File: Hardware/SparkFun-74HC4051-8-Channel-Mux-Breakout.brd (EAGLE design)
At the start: 12.7 x 27.9 mm, 12 parts, among them U1 74HC4051BQ

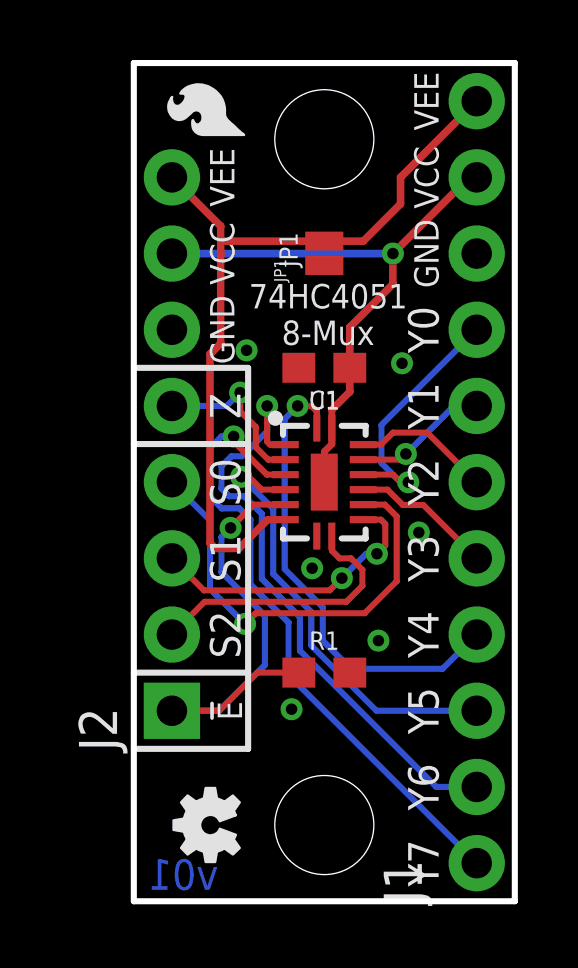
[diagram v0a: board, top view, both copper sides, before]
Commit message: Resolving issues flagged on issue 1.
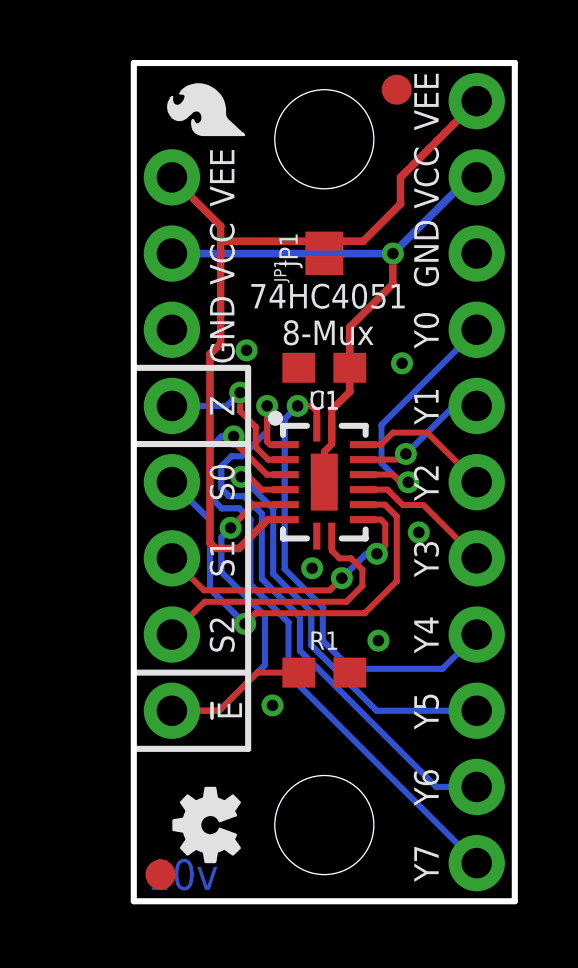
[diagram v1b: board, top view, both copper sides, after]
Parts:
- added FD1, FD2: FIDUCIAL1X2, SparkFun-Aesthetics:FIDUCIAL-1X2
- J1: device SparkFun-Connectors:1X11_NO_SILK -> SparkFun-Connectors:1X11
- J2: device SparkFun-Connectors:1X08_PIN1_NO_SILK -> SparkFun-Connectors:1X08_ROUND
- moved FRAME1 33.6 mm to (-20.3, -12.7)
- flipped J1 to the bottom
- flipped J2 to the bottom
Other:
- board text added: "Jim Lindblom"

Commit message: Few changes after running the checklist.
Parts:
- moved FRAME1 10.9 mm to (-16.5, -22.9)
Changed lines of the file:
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@@
 <wire x1="0" y1="5.08" x2="3.81" y2="5.08" width="0.2032" layer="21"/>
 <wire x1="3.81" y1="5.08" x2="3.81" y2="7.62" width="0.2032" layer="21"/>
-<text x="1.651" y="0.381" size="1.016" layer="16" font="vector" ratio="15" rot="MR0" align="bottom-center">v01</text>
+<text x="1.651" y="0.381" size="1.016" layer="16" font="vector" ratio="20" rot="MR0" align="bottom-center">v01</text>
 <wire x1="0" y1="17.78" x2="3.937" y2="17.78" width="0.2032" layer="22"/>
 <wire x1="3.937" y1="17.78" x2="3.937" y2="15.24" width="0.2032" layer="22"/>
@@
 <wire x1="3.937" y1="5.08" x2="0" y2="5.08" width="0.2032" layer="22"/>
 <wire x1="3.937" y1="5.08" x2="3.937" y2="7.62" width="0.2032" layer="22"/>
-<text x="10.16" y="-12.7" size="1.778" layer="51" font="vector" ratio="15">Jim Lindblom</text>
+<text x="13.97" y="-22.86" size="1.778" layer="51" font="vector" ratio="15">Jim Lindblom</text>
+<dimension x1="0" y1="0" x2="6.35" y2="2.54" x3="-1.27" y3="1.27" textsize="1.016" textratio="15" layer="47" dtype="vertical" unit="inch" precision="3"/>
+<dimension x1="0" y1="0" x2="1.27" y2="6.35" x3="-3.81" y3="3.175" textsize="1.016" textratio="15" layer="47" dtype="vertical" unit="inch" precision="3"/>
+<dimension x1="0" y1="0" x2="6.35" y2="25.4" x3="-6.35" y3="12.7" textsize="1.016" textratio="15" layer="47" dtype="vertical" unit="inch" precision="3"/>
+<dimension x1="0" y1="0" x2="0" y2="27.94" x3="-8.89" y3="13.97" textsize="1.016" textratio="15" layer="47" dtype="vertical" unit="inch" precision="3"/>
+<dimension x1="0" y1="0" x2="1.27" y2="6.35" x3="0.635" y3="-2.54" textsize="0.889" textratio="15" layer="47" dtype="horizontal" unit="inch" precision="3"/>
+<dimension x1="0" y1="0" x2="6.35" y2="2.54" x3="3.175" y3="-5.08" textsize="1.016" textratio="15" layer="47" dtype="horizontal" unit="inch" precision="3"/>
+<dimension x1="0" y1="0" x2="11.43" y2="1.27" x3="5.715" y3="-7.62" textsize="1.016" textratio="15" layer="47" dtype="horizontal" unit="inch" precision="3"/>
+<dimension x1="0" y1="0" x2="12.7" y2="0" x3="6.35" y3="-10.16" textsize="1.016" textratio="15" layer="47" dtype="horizontal" unit="inch" precision="3"/>
 </plain>
 <attributes>
@@
 <attribute name="PROD_ID" value="CAP-00810" x="6.35" y="17.78" size="1.778" layer="27" rot="R180" display="off"/>
 </element>
-<element name="FRAME1" library="SparkFun-Aesthetics" package="CREATIVE_COMMONS" value="FRAME-LETTER" x="-20.32" y="-12.7"/>
+<element name="FRAME1" library="SparkFun-Aesthetics" package="CREATIVE_COMMONS" value="FRAME-LETTER" x="-16.51" y="-22.86"/>
 <element name="J1" library="SparkFun-Connectors" package="1X11" value="" x="11.43" y="1.27" rot="MR90"/>
 <element name="J2" library="SparkFun-Connectors" package="1X08_ROUND" value="" x="1.27" y="6.35" rot="MR90">
 <attribute name="PROD_ID" value="CONN-08437" x="1.27" y="6.35" size="1.778" layer="28" rot="MR90" display="off"/>
 </element>
-<element name="U1" library="8mux" package="DHVQFN-16-2.5X3.5MM" value="74HC4051BQ" x="6.35" y="13.97" rot="R270"/>
+<element name="U1" library="8mux" package="DHVQFN-16-2.5X3.5MM" value="74HC4051BQ" x="6.35" y="13.97" rot="R270">
+<attribute name="PROD_ID" value="IC-13334" x="6.35" y="13.97" size="1.778" layer="27" rot="R270" display="off"/>
+</element>
 <element name="R1" library="SparkFun-Resistors" package="0603" value="100k" x="6.35" y="7.62">
 <attribute name="PROD_ID" value="RES-07828" x="6.35" y="7.62" size="1.778" layer="27" font="vector" ratio="15" display="off"/>
@@
 <via x="8.9408" y="17.9324" extent="1-16" drill="0.381"/>
 <via x="5.9436" y="11.0998" extent="1-16" drill="0.381"/>
-<via x="8.1534" y="8.6868" extent="1-16" drill="0.381"/>
+<via x="9.1694" y="9.8298" extent="1-16" drill="0.381"/>
 <via x="4.6228" y="6.5278" extent="1-16" drill="0.381"/>
 <contactref element="JP1" pad="1"/>

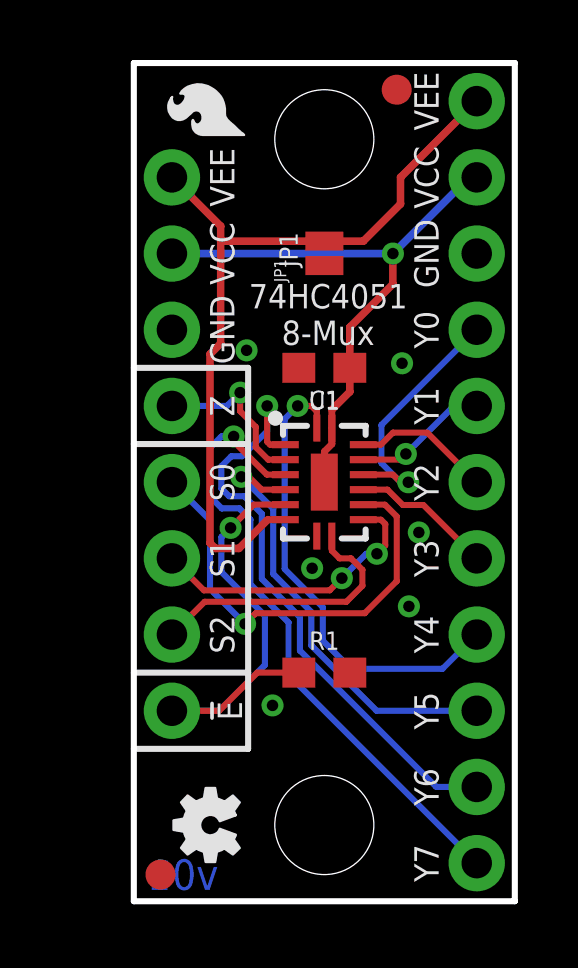
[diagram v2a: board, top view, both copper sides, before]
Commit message: Fixing silkscreen, upping to v10
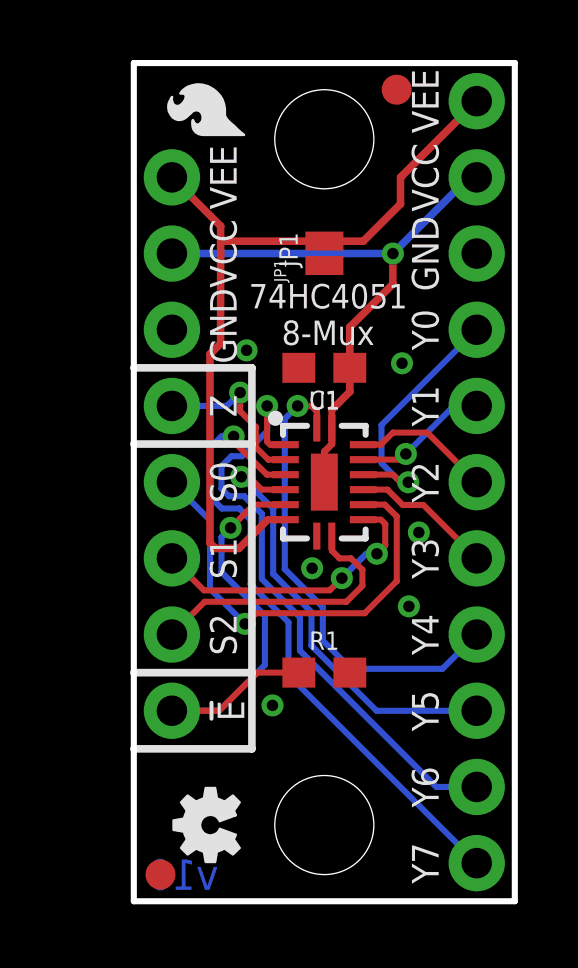
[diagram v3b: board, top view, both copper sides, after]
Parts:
- moved LOGO3 4.20 mm to (5.65, 3.94)
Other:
- board text added: "74HC4051 8-Channel"
- board text added: "Mux/Demux"
- board text added: "v10"
- board text removed: "74HC4051 8-Channel Analog Mux/Demux"
- board text removed: "v01"

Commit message: Swapping 100k resistor out with 10k
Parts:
- R1: value 100k -> 10k
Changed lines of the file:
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@@
 <setting verticaltext="up"/>
 </settings>
-<grid distance="0.05" unitdist="inch" unit="inch" style="lines" multiple="1" display="yes" altdistance="0.0025" altunitdist="inch" altunit="inch"/>
+<grid distance="0.05" unitdist="inch" unit="inch" style="lines" multiple="1" display="yes" altdistance="0.005" altunitdist="inch" altunit="inch"/>
 <layers>
 <layer number="1" name="Top" color="4" fill="1" visible="yes" active="yes"/>
@@
 <layer number="47" name="Measures" color="7" fill="1" visible="no" active="yes"/>
 <layer number="48" name="Document" color="7" fill="1" visible="no" active="yes"/>
-<layer number="49" name="Reference" color="7" fill="1" visible="yes" active="yes"/>
+<layer number="49" name="Reference" color="7" fill="1" visible="no" active="yes"/>
 <layer number="50" name="dxf" color="7" fill="1" visible="no" active="no"/>
 <layer number="51" name="tDocu" color="6" fill="1" visible="yes" active="yes"/>
@@
 <attribute name="PROD_ID" value="IC-13334" x="6.35" y="13.97" size="1.778" layer="27" rot="R270" display="off"/>
 </element>
-<element name="R1" library="SparkFun-Resistors" package="0603" value="100k" x="6.35" y="7.62">
-<attribute name="PROD_ID" value="RES-07828" x="6.35" y="7.62" size="1.778" layer="27" font="vector" ratio="15" display="off"/>
+<element name="R1" library="SparkFun-Resistors" package="0603" value="10k" x="6.35" y="7.62">
+<attribute name="PROD_ID" value="RES-00824" x="6.35" y="7.62" size="1.778" layer="27" font="vector" ratio="15" display="off"/>
 </element>
 <element name="H1" library="SparkFun-Electromechanical" package="STAND-OFF" value="STAND-OFF" x="6.35" y="25.4"/>
